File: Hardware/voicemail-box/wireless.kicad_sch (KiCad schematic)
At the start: 9 parts, among them J5 Conn_02x06_Top_Bottom, U1 ESP32-WROOM-32

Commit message: ~working on first pcb-Draft
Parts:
- added J1: Conn_01x04_Pin, Connector_PinHeader_2.54mm:PinHeader_1x04_P2.54mm_Vertical, symbol Connector:Conn_01x04_Pin
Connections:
- net GND: now also J1.3 (Pin_3)
- net IO0: now also J1.4 (Pin_4)
- net RXD0: now also J1.2 (Pin_2)
- net TXD0: now also J1.1 (Pin_1)
- no-connect marks 26 -> 24
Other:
- note added: "ESP32 flash"
- note removed: "?"
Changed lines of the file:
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@@
 	(generator_version "9.0")
 	(paper "A4")
-	(text "?"
-		(exclude_from_sim no)
-		(at 232.664 66.04 0)
-		(effects
-			(font
-				(size 2.54 2.54)
-			)
-			(justify left)
-		)
-	)
 	(text "Pmod ESP32\n- WiFi\n- BLE\n- Bt 4.1 Interface"
 		(exclude_from_sim no)
 		(at 126.746 81.534 0)
+		(effects
+			(font
+				(size 0.635 0.635)
+			)
+			(justify left)
+		)
+	)
+	(text "ESP32 flash"
+		(exclude_from_sim no)
+		(at 248.412 65.024 0)
 		(effects
 			(font
@@
 	)
 	(junction
+		(at 223.52 77.47)
+		(diameter 0)
+		(color 0 0 0 0)
+	)
+	(junction
 		(at 205.74 67.31)
 		(diameter 0)
@@
 	)
 	(no_connect
-		(at 208.28 69.85)
-	)
-	(no_connect
 		(at 198.12 82.55)
 	)
@@
 	)
 	(no_connect
-		(at 208.28 74.93)
-	)
-	(no_connect
 		(at 198.12 123.19)
 	)
@@
 	(wire
 		(pts
+			(xy 247.65 69.85) (xy 231.14 69.85)
+		)
+		(stroke
+			(width 0)
+			(type default)
+		)
+	)
+	(wire
+		(pts
 			(xy 165.1 58.42) (xy 170.18 58.42)
 		)
@@
 	(wire
 		(pts
+			(xy 231.14 69.85) (xy 231.14 77.47)
+		)
+		(stroke
+			(width 0)
+			(type default)
+		)
+	)
+	(wire
+		(pts
 			(xy 165.1 58.42) (xy 165.1 57.15)
 		)
@@
 	(wire
 		(pts
+			(xy 223.52 77.47) (xy 223.52 78.74)
+		)
+		(stroke
+			(width 0)
+			(type default)
+		)
+	)
+	(wire
+		(pts
 			(xy 116.84 77.47) (xy 123.19 77.47)
 		)
@@
 	(wire
 		(pts
+			(xy 247.65 74.93) (xy 237.49 74.93)
+		)
+		(stroke
+			(width 0)
+			(type default)
+		)
+	)
+	(wire
+		(pts
 			(xy 74.93 90.17) (xy 81.28 90.17)
 		)
@@
 	(wire
 		(pts
+			(xy 223.52 77.47) (xy 231.14 77.47)
+		)
+		(stroke
+			(width 0)
+			(type default)
+		)
+	)
+	(wire
+		(pts
 			(xy 215.9 113.03) (xy 198.12 113.03)
 		)
@@
 	(wire
 		(pts
-			(xy 223.52 67.31) (xy 231.14 67.31)
+			(xy 247.65 72.39) (xy 237.49 72.39)
+		)
+		(stroke
+			(width 0)
+			(type default)
+		)
+	)
+	(wire
+		(pts
+			(xy 223.52 67.31) (xy 247.65 67.31)
 		)
 		(stroke
@@
 		)
 	)
+	(label "TXD0"
+		(at 247.65 74.93 180)
+		(effects
+			(font
+				(size 1.27 1.27)
+			)
+			(justify right bottom)
+		)
+	)
 	(label "MISO"
 		(at 215.9 100.33 180)
@@
 	(label "IO0"
 		(at 231.14 67.31 180)
+		(effects
+			(font
+				(size 1.27 1.27)
+			)
+			(justify right bottom)
+		)
+	)
+	(label "RXD0"
+		(at 247.65 72.39 180)
 		(effects
 			(font
@@
 				(path "/e63e39d7-6ac0-4ffd-8aa3-1841a4541b55/c4907074-0e50-41f9-8f09-d9d4d6cc7ba3"
 					(reference "C2")
+					(unit 1)
+				)
+			)
+		)
+	)
+	(symbol
+		(lib_id "Connector:Conn_01x04_Pin")
+		(at 252.73 72.39 180)
+		(unit 1)
+		(exclude_from_sim no)
+		(in_bom yes)
+		(on_board yes)
+		(dnp no)
+		(fields_autoplaced yes)
+		(property "Reference" "J1"
+			(at 254 69.8499 0)
+			(effects
+				(font
+					(size 1.27 1.27)
+				)
+				(justify right)
+			)
+		)
+		(property "Value" "Conn_01x04_Pin"
+			(at 254 72.3899 0)
+			(effects
+				(font
+					(size 1.27 1.27)
+				)
+				(justify right)
+			)
+		)
+		(property "Footprint" "Connector_PinHeader_2.54mm:PinHeader_1x04_P2.54mm_Vertical"
+			(at 252.73 72.39 0)
+			(effects
+				(font
+					(size 1.27 1.27)
+				)
+				(hide yes)
+			)
+		)
+		(property "Datasheet" "~"
+			(at 252.73 72.39 0)
+			(effects
+				(font
+					(size 1.27 1.27)
+				)
+				(hide yes)
+			)
+		)
+		(property "Description" "Generic connector, single row, 01x04, script generated"
+			(at 252.73 72.39 0)
+			(effects
+				(font
+					(size 1.27 1.27)
+				)
+				(hide yes)
+			)
+		)
+		(pin "2"
+		)
+		(pin "4"
+		)
+		(pin "3"
+		)
+		(pin "1"
+		)
+		(instances
+			(project ""
+				(path "/e63e39d7-6ac0-4ffd-8aa3-1841a4541b55/c4907074-0e50-41f9-8f09-d9d4d6cc7ba3"
+					(reference "J1")
 					(unit 1)
 				)
@@
 		(lib_name "GND_1")
 		(lib_id "power:GND")
-		(at 223.52 77.47 0)
+		(at 223.52 78.74 0)
 		(unit 1)
 		(exclude_from_sim no)
@@
 		(fields_autoplaced yes)
 		(property "Reference" "#PWR011"
+			(at 223.52 85.09 0)
+			(effects
+				(font
+					(size 1.27 1.27)
+				)
+				(hide yes)
+			)
+		)
+		(property "Value" "GND"
 			(at 223.52 83.82 0)
 			(effects
@@
 					(size 1.27 1.27)
 				)
-				(hide yes)
-			)
-		)
-		(property "Value" "GND"
-			(at 223.52 82.55 0)
-			(effects
-				(font
-					(size 1.27 1.27)
-				)
 			)
 		)
 		(property "Footprint" ""
-			(at 223.52 77.47 0)
+			(at 223.52 78.74 0)
 			(effects
 				(font
@@
 		)
 		(property "Datasheet" ""
-			(at 223.52 77.47 0)
+			(at 223.52 78.74 0)
 			(effects
 				(font
@@
 		)
 		(property "Description" "Power symbol creates a global label with name \"GND\" , ground"
-			(at 223.52 77.47 0)
-			(effects
-				(font
+			(at 223.52 78.74 0)
+			(effects
+				(font

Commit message: -
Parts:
- RN1: value np_0R -> 0R
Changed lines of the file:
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@@
 			)
 		)
-		(property "Value" "np_0R"
+		(property "Value" "0R"
 			(at 86.36 60.96 90)
 			(effects

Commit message: schematic draft
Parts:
- RN301: renamed from RN1; value 0R -> np_0R
- renumbered C1 to C301, C2 to C302, J5 to J301, J1 to J302, R1 to R301, R2 to R302, R3 to R303, RN2 to RN302, U1 to U301
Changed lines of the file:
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@@
+	(wire
+		(pts
+			(xy 237.49 72.39) (xy 247.65 72.39)
+		)
+		(stroke
+			(width 0)
+			(type default)
+		)
+	)
 	(wire
 		(pts
@@
 	(wire
 		(pts
+			(xy 237.49 74.93) (xy 247.65 74.93)
+		)
+		(stroke
+			(width 0)
+			(type default)
+		)
+	)
+	(wire
+		(pts
 			(xy 142.24 48.26) (xy 142.24 77.47)
 		)
@@
 	(wire
 		(pts
-			(xy 247.65 74.93) (xy 237.49 74.93)
-		)
-		(stroke
-			(width 0)
-			(type default)
-		)
-	)
-	(wire
-		(pts
 			(xy 74.93 90.17) (xy 81.28 90.17)
 		)
@@
 		(pts
 			(xy 74.93 69.85) (xy 81.28 69.85)
-		)
-		(stroke
-			(width 0)
-			(type default)
-		)
-	)
-	(wire
-		(pts
-			(xy 247.65 72.39) (xy 237.49 72.39)
 		)
 		(stroke
@@
 		)
 	)
+	(label "RXD0"
+		(at 237.49 72.39 0)
+		(effects
+			(font
+				(size 1.27 1.27)
+			)
+			(justify left bottom)
+		)
+	)
 	(label "TXD{slash}MISO"
 		(at 105.41 69.85 0)
@@
 	)
 	(label "TXD0"
-		(at 247.65 74.93 180)
-		(effects
-			(font
-				(size 1.27 1.27)
-			)
-			(justify right bottom)
+		(at 237.49 74.93 0)
+		(effects
+			(font
+				(size 1.27 1.27)
+			)
+			(justify left bottom)
 		)
 	)
@@
 	(label "IO0"
 		(at 231.14 67.31 180)
-		(effects
-			(font
-				(size 1.27 1.27)
-			)
-			(justify right bottom)
-		)
-	)
-	(label "RXD0"
-		(at 247.65 72.39 180)
 		(effects
 			(font
@@
 		(on_board yes)
 		(dnp no)
-		(property "Reference" "C1"
+		(property "Reference" "C301"
 			(at 166.116 50.8 0)
 			(effects
@@
 			(project "voicemail-box"
 				(path "/e63e39d7-6ac0-4ffd-8aa3-1841a4541b55/c4907074-0e50-41f9-8f09-d9d4d6cc7ba3"
-					(reference "C1")
+					(reference "C301")
 					(unit 1)
 				)
@@
 		(on_board yes)
 		(dnp no)
-		(property "Reference" "C2"
-			(at 178.308 50.546 0)
+		(property "Reference" "C302"
+			(at 177.8 50.546 0)
 			(effects
 				(font
@@
 			(project "voicemail-box"
 				(path "/e63e39d7-6ac0-4ffd-8aa3-1841a4541b55/c4907074-0e50-41f9-8f09-d9d4d6cc7ba3"
-					(reference "C2")
+					(reference "C302")
 					(unit 1)
 				)
@@
 		(dnp no)
 		(fields_autoplaced yes)
-		(property "Reference" "J1"
+		(property "Reference" "J302"
 			(at 254 69.8499 0)
 			(effects
@@
 			(project ""
 				(path "/e63e39d7-6ac0-4ffd-8aa3-1841a4541b55/c4907074-0e50-41f9-8f09-d9d4d6cc7ba3"
-					(reference "J1")
+					(reference "J302")
 					(unit 1)
 				)
@@
 		(dnp no)
 		(fields_autoplaced yes)
-		(property "Reference" "R3"
+		(property "Reference" "R303"
 			(at 226.06 71.1199 0)
 			(effects
@@
 			(project "voicemail-box"
 				(path "/e63e39d7-6ac0-4ffd-8aa3-1841a4541b55/c4907074-0e50-41f9-8f09-d9d4d6cc7ba3"
-					(reference "R3")
+					(reference "R303")
 					(unit 1)
 				)
@@
 		(dnp no)
 		(fields_autoplaced yes)
-		(property "Reference" "R2"
+		(property "Reference" "R302"
 			(at 208.28 57.1499 0)
 			(effects
@@
 			(project "voicemail-box"
 				(path "/e63e39d7-6ac0-4ffd-8aa3-1841a4541b55/c4907074-0e50-41f9-8f09-d9d4d6cc7ba3"
-					(reference "R2")
+					(reference "R302")
 					(unit 1)
 				)
@@
 		(dnp no)
 		(fields_autoplaced yes)
-		(property "Reference" "R1"
+		(property "Reference" "R301"
 			(at 160.02 57.1499 0)
 			(effects
@@
 			(project "voicemail-box"
 				(path "/e63e39d7-6ac0-4ffd-8aa3-1841a4541b55/c4907074-0e50-41f9-8f09-d9d4d6cc7ba3"
-					(reference "R1")
+					(reference "R301")
 					(unit 1)
 				)
@@
 		(dnp no)
 		(fields_autoplaced yes)
-		(property "Reference" "#PWR010"
+		(property "Reference" "#PWR0304"
 			(at 182.88 140.97 0)
 			(effects
@@
 			(project "voicemail-box"
 				(path "/e63e39d7-6ac0-4ffd-8aa3-1841a4541b55/c4907074-0e50-41f9-8f09-d9d4d6cc7ba3"
-					(reference "#PWR010")
+					(reference "#PWR0304")
 					(unit 1)
 				)
@@
 		(on_board yes)
 		(dnp no)
-		(property "Reference" "U1"
+		(property "Reference" "U301"
 			(at 185.42 61.214 0)
 			(effects
@@
 			(project "voicemail-box"
 				(path "/e63e39d7-6ac0-4ffd-8aa3-1841a4541b55/c4907074-0e50-41f9-8f09-d9d4d6cc7ba3"
-					(reference "U1")
+					(reference "U301")
 					(unit 1)
 				)
@@
 		(dnp no)
 		(fields_autoplaced yes)
-		(property "Reference" "#PWR09"
+		(property "Reference" "#PWR0303"
 			(at 182.88 50.8 0)
 			(effects
@@
 			(project "voicemail-box"
 				(path "/e63e39d7-6ac0-4ffd-8aa3-1841a4541b55/c4907074-0e50-41f9-8f09-d9d4d6cc7ba3"
-					(reference "#PWR09")
+					(reference "#PWR0303")
 					(unit 1)
 				)
@@
 		(dnp no)
 		(fields_autoplaced yes)
-		(property "Reference" "#PWR07"
+		(property "Reference" "#PWR0301"
 			(at 129.54 93.98 0)
 			(effects
@@
 			(project "voicemail-box"
 				(path "/e63e39d7-6ac0-4ffd-8aa3-1841a4541b55/c4907074-0e50-41f9-8f09-d9d4d6cc7ba3"
-					(reference "#PWR07")
+					(reference "#PWR0301")
 					(unit 1)
 				)
@@
 		(on_board yes)
 		(dnp no)
-		(property "Reference" "#PWR08"
+		(property "Reference" "#PWR0302"
 			(at 170.18 66.04 0)
 			(effects
@@
 			(project "voicemail-box"
 				(path "/e63e39d7-6ac0-4ffd-8aa3-1841a4541b55/c4907074-0e50-41f9-8f09-d9d4d6cc7ba3"
-					(reference "#PWR08")
+					(reference "#PWR0302")
 					(unit 1)
 				)
@@
 		(on_board yes)
 		(dnp no)
-		(property "Reference" "J5"
+		(property "Reference" "J301"
 			(at 129.54 58.42 0)
 			(effects
@@
 			(project "voicemail-box"
 				(path "/e63e39d7-6ac0-4ffd-8aa3-1841a4541b55/c4907074-0e50-41f9-8f09-d9d4d6cc7ba3"
-					(reference "J5")
+					(reference "J301")
 					(unit 1)
 				)
@@
 		(dnp no)
 		(fields_autoplaced yes)
-		(property "Reference" "#PWR011"
+		(property "Reference" "#PWR0305"
 			(at 223.52 85.09 0)
 			(effects
@@
 			(project "voicemail-box"
 				(path "/e63e39d7-6ac0-4ffd-8aa3-1841a4541b55/c4907074-0e50-41f9-8f09-d9d4d6cc7ba3"
-					(reference "#PWR011")
+					(reference "#PWR0305")
 					(unit 1)
 				)
@@
 		(dnp no)
 		(fields_autoplaced yes)
-		(property "Reference" "RN2"
+		(property "Reference" "RN302"
 			(at 86.36 76.2 90)
 			(effects
@@
 			(project "voicemail-box"
 				(path "/e63e39d7-6ac0-4ffd-8aa3-1841a4541b55/c4907074-0e50-41f9-8f09-d9d4d6cc7ba3"
-					(reference "RN2")
+					(reference "RN302")
 					(unit 1)
 				)
@@
 		(dnp no)
 		(fields_autoplaced yes)
-		(property "Reference" "RN1"
+		(property "Reference" "RN301"
 			(at 86.36 58.42 90)
 			(effects
@@
 			)
 		)
-		(property "Value" "0R"
+		(property "Value" "np_0R"
 			(at 86.36 60.96 90)
 			(effects
@@
 			(project "voicemail-box"
 				(path "/e63e39d7-6ac0-4ffd-8aa3-1841a4541b55/c4907074-0e50-41f9-8f09-d9d4d6cc7ba3"
-					(reference "RN1")
+					(reference "RN301")
 					(unit 1)
 				)

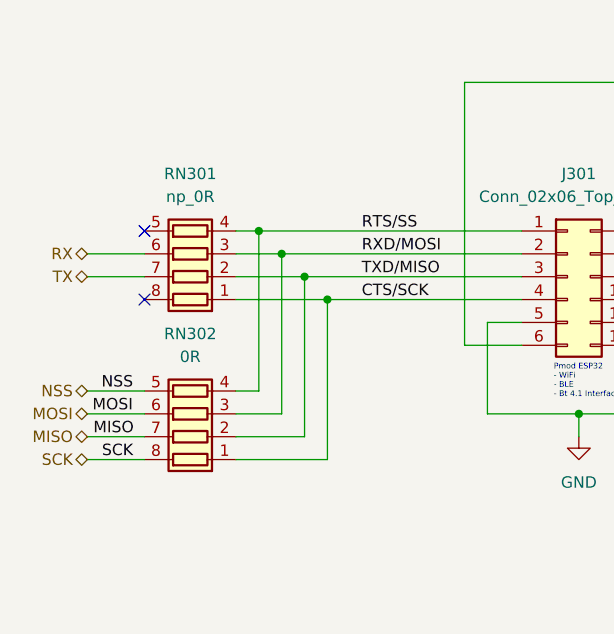
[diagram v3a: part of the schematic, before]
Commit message: HW Layout progress todo: + Antenna + Audio Jacks + Planes (Supply only)
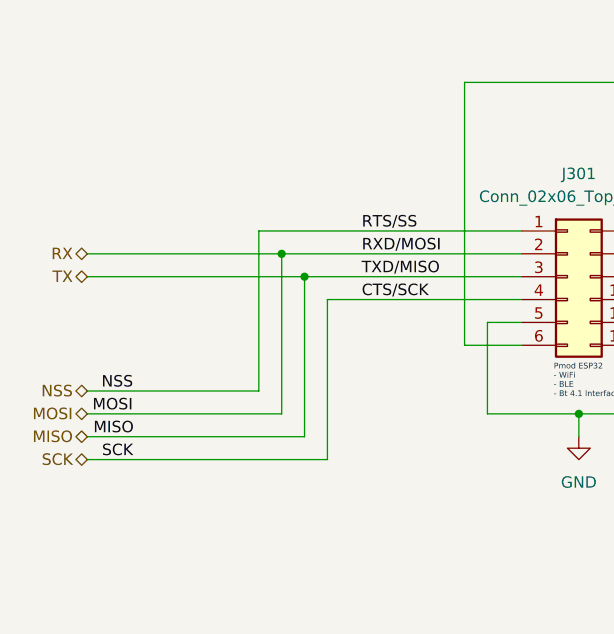
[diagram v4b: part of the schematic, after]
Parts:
- removed RN301: np_0R, Resistor_SMD:R_Array_Convex_4x0603, symbol Device:R_Pack04
- removed RN302: 0R, Resistor_SMD:R_Array_Convex_4x0603, symbol Device:R_Pack04
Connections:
- net CTS/SCK is gone; now on net SCK: J301.4 (Pin_4)
- net RTS/SS is gone; now on net NSS: J301.1 (Pin_1)
- net RX is gone; now on net MOSI: U301.27 (IO16)
- net RXD/MOSI is gone; now on net MOSI: J301.2 (Pin_2)
- net TX is gone; now on net MISO: U301.28 (IO17)
- net TXD/MISO is gone; now on net MISO: J301.3 (Pin_3)
- no-connect marks 24 -> 22

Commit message: schema review
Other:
- note added: "ESP32 Prog"
- note removed: "ESP32 flash"
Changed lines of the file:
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@@
 	(text "Pmod ESP32\n- WiFi\n- BLE\n- Bt 4.1 Interface"
 		(exclude_from_sim no)
-		(at 126.746 81.534 0)
-		(effects
-			(font
-				(size 0.635 0.635)
+		(at 120.904 84.074 0)
+		(effects
+			(font
+				(size 1.27 1.27)
 			)
 			(justify left)
 		)
 	)
-	(text "ESP32 flash"
+	(text "ESP32 Prog"
 		(exclude_from_sim no)
-		(at 248.412 65.024 0)
-		(effects
-			(font
-				(size 0.635 0.635)
+		(at 248.666 64.008 0)
+		(effects
+			(font
+				(size 1.27 1.27)
 			)
 			(justify left)
@@
 	)
 	(junction
-		(at 129.54 85.09)
+		(at 129.54 90.17)
 		(diameter 0)
 		(color 0 0 0 0)
@@
 	(wire
 		(pts
-			(xy 139.7 85.09) (xy 139.7 74.93)
+			(xy 139.7 90.17) (xy 139.7 74.93)
 		)
 		(stroke
@@
 	(wire
 		(pts
-			(xy 119.38 85.09) (xy 119.38 74.93)
+			(xy 119.38 90.17) (xy 119.38 74.93)
 		)
 		(stroke
@@
 	(wire
 		(pts
-			(xy 129.54 85.09) (xy 119.38 85.09)
+			(xy 129.54 90.17) (xy 119.38 90.17)
 		)
 		(stroke
@@
 	(wire
 		(pts
-			(xy 129.54 87.63) (xy 129.54 85.09)
+			(xy 129.54 92.71) (xy 129.54 90.17)
 		)
 		(stroke
@@
 	(wire
 		(pts
-			(xy 129.54 85.09) (xy 139.7 85.09)
+			(xy 129.54 90.17) (xy 139.7 90.17)
 		)
 		(stroke
@@
 		(lib_name "GND_1")
 		(lib_id "power:GND")
-		(at 129.54 87.63 0)
+		(at 129.54 92.71 0)
 		(unit 1)
 		(exclude_from_sim no)
@@
 		(fields_autoplaced yes)
 		(property "Reference" "#PWR0301"
-			(at 129.54 93.98 0)
+			(at 129.54 99.06 0)
 			(effects
 				(font
@@
 		)
 		(property "Value" "GND"
+			(at 129.54 97.79 0)
+			(effects
+				(font
+					(size 1.27 1.27)
+				)
+			)
+		)
+		(property "Footprint" ""
 			(at 129.54 92.71 0)
 			(effects
@@
 					(size 1.27 1.27)
 				)
-			)
-		)
-		(property "Footprint" ""
-			(at 129.54 87.63 0)
-			(effects
-				(font
-					(size 1.27 1.27)
-				)
 				(hide yes)
 			)
 		)
 		(property "Datasheet" ""
-			(at 129.54 87.63 0)
+			(at 129.54 92.71 0)
 			(effects
 				(font
@@
 		)
 		(property "Description" "Power symbol creates a global label with name \"GND\" , ground"
-			(at 129.54 87.63 0)
-			(effects
-				(font
+			(at 129.54 92.71 0)
+			(effects
+				(font

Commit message: ~layout
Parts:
- removed J302: Conn_01x04_Pin, Connector_PinHeader_2.54mm:PinHeader_1x04_P2.54mm_Vertical, symbol Connector:Conn_01x04_Pin
- added J303: Conn_01x06, Connector_PinHeader_2.54mm:PinHeader_1x06_P2.54mm_Vertical, symbol Connector_Generic:Conn_01x06
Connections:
- net +3V3: now also J303.1 (Pin_1)
- net GND: now also J303.3 (Pin_3), J303.6 (Pin_6)
- net IO0: now also J303.2 (Pin_2)
- net RXD0: now also J303.4 (Pin_4)
- net TXD0: now also J303.5 (Pin_5)
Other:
- note added: "set Boot-mode (2) to high"
- moved on the sheet: C301, C302, J301, R301, R302, R303, U301

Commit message: + Abstract
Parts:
- added J302: Conn_02x06_Odd_Even, symbol Connector_Generic:Conn_02x06_Odd_Even
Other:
- note added: "Compare"
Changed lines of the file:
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@@
+		)
+	)
+	(text "Compare"
+		(exclude_from_sim no)
+		(at 120.396 26.162 0)
+		(effects
+			(font
+				(size 1.27 1.27)
+			)
+			(justify left)
 		)
 	)
@@
 					(unit 1)
 				)
+			)
+		)
+	)
+	(symbol
+		(lib_id "Connector_Generic:Conn_02x06_Odd_Even")
+		(at 107.95 26.67 0)
+		(unit 1)
+		(exclude_from_sim no)
+		(in_bom yes)
+		(on_board yes)
+		(dnp no)
+		(fields_autoplaced yes)
+		(property "Reference" "J302"
+			(at 109.22 15.24 0)
+			(effects
+				(font
+					(size 1.27 1.27)
+				)
+			)
+		)
+		(property "Value" "Conn_02x06_Odd_Even"
+			(at 109.22 17.78 0)
+			(effects
+				(font
+					(size 1.27 1.27)
+				)
+			)
+		)
+		(property "Footprint" ""
+			(at 107.95 26.67 0)
+			(effects
+				(font
+					(size 1.27 1.27)
+				)
+				(hide yes)
+			)
+		)
+		(property "Datasheet" "~"
+			(at 107.95 26.67 0)
+			(effects
+				(font
+					(size 1.27 1.27)
+				)
+				(hide yes)
+			)
+		)
+		(property "Description" "Generic connector, double row, 02x06, odd/even pin numbering scheme (row 1 odd numbers, row 2 even numbers), script generated (kicad-library-utils/schlib/autogen/connector/)"
+			(at 107.95 26.67 0)
+			(effects
+				(font
+					(size 1.27 1.27)
+				)
+				(hide yes)
+			)
+		)
+		(pin "8"
+		)
+		(pin "7"
+		)
+		(pin "6"
+		)
+		(pin "11"
+		)
+		(pin "9"
+		)
+		(pin "4"
+		)
+		(pin "5"
+		)
+		(pin "1"
+		)
+		(pin "3"
+		)
+		(pin "10"
+		)
+		(pin "12"
+		)
+		(pin "2"
+		)
+		(instances
+			(project ""
+				(path "/e63e39d7-6ac0-4ffd-8aa3-1841a4541b55/c4907074-0e50-41f9-8f09-d9d4d6cc7ba3"
+					(reference "J302")
+					(unit 1)
+				)
